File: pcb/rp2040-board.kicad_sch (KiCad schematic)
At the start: 4 parts, among them U1 RP2040, U2 W25Q128JVS

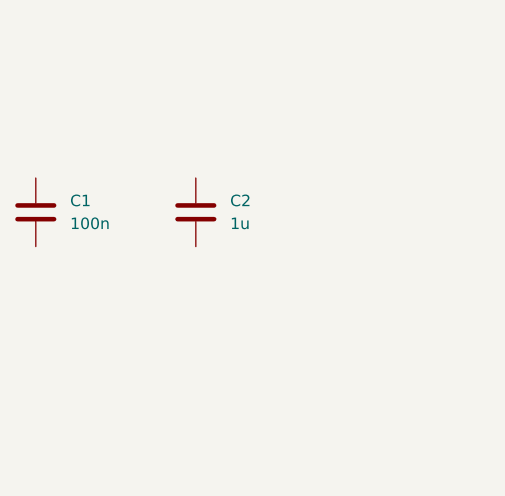
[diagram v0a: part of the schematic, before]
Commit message: add more parts to the BOM
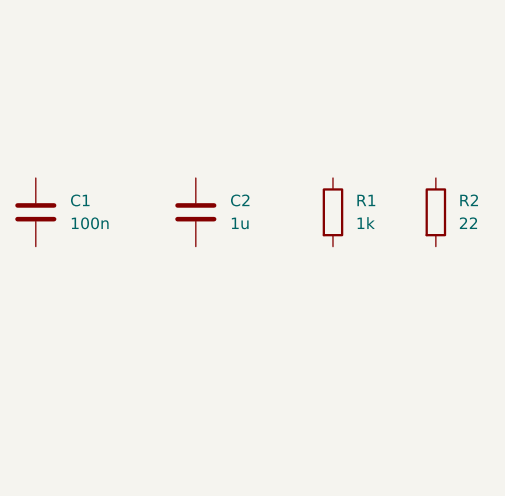
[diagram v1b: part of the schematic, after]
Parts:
- added R1: 1k, Resistor_SMD:R_0402_1005Metric, symbol Device:R
- added R2: 22, Resistor_SMD:R_0402_1005Metric, symbol Device:R
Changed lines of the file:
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@@
+    )
+  )
+  (symbol (lib_id "Device:R") (at 261.62 67.31 0) (unit 1)
+    (in_bom yes) (on_board yes) (dnp no) (fields_autoplaced)
+    (property "Reference" "R2" (at 264.16 66.04 0)
+      (effects (font (size 1.27 1.27)) (justify left))
+    )
+    (property "Value" "22" (at 264.16 68.58 0)
+      (effects (font (size 1.27 1.27)) (justify left))
+    )
+    (property "Footprint" "Resistor_SMD:R_0402_1005Metric" (at 259.842 67.31 90)
+      (effects (font (size 1.27 1.27)) hide)
+    )
+    (property "Datasheet" "https://datasheet.lcsc.com/lcsc/2205311900_UNI-ROYAL-Uniroyal-Elec-0402WGF220JTCE_C25092.pdf" (at 261.62 67.31 0)
+      (effects (font (size 1.27 1.27)) hide)
+    )
+    (property "LCSC Part" "C25092" (at 261.62 67.31 0)
+      (effects (font (size 1.27 1.27)) hide)
+    )
+    (pin "1")
+    (pin "2")
+    (instances
+      (project "rp2040-board"
+        (path "/75fe2d07-4ff9-4014-b967-9ecbb30e480e"
+          (reference "R2") (unit 1)
+        )
+      )
+    )
+  )
+  (symbol (lib_id "Device:R") (at 250.19 67.31 0) (unit 1)
+    (in_bom yes) (on_board yes) (dnp no) (fields_autoplaced)
+    (property "Reference" "R1" (at 252.73 66.04 0)
+      (effects (font (size 1.27 1.27)) (justify left))
+    )
+    (property "Value" "1k" (at 252.73 68.58 0)
+      (effects (font (size 1.27 1.27)) (justify left))
+    )
+    (property "Footprint" "Resistor_SMD:R_0402_1005Metric" (at 248.412 67.31 90)
+      (effects (font (size 1.27 1.27)) hide)
+    )
+    (property "Datasheet" "https://datasheet.lcsc.com/lcsc/2206010216_UNI-ROYAL-Uniroyal-Elec-0402WGF1001TCE_C11702.pdf" (at 250.19 67.31 0)
+      (effects (font (size 1.27 1.27)) hide)
+    )
+    (property "LCSC Part" "C11702" (at 250.19 67.31 0)
+      (effects (font (size 1.27 1.27)) hide)
+    )
+    (pin "1")
+    (pin "2")
+    (instances
+      (project "rp2040-board"
+        (path "/75fe2d07-4ff9-4014-b967-9ecbb30e480e"
+          (reference "R1") (unit 1)
+        )
+      )
     )
   )

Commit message: schematic wip
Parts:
- added C10, C11, C12, C3, C5, C6, C7, C8, C9: 100n, Capacitor_SMD:C_0402_1005Metric, symbol Device:C
- added C13, C4: 1u, Capacitor_SMD:C_0402_1005Metric, symbol Device:C
- added R3: 22, Resistor_SMD:R_0402_1005Metric, symbol Device:R
- added R4: DNP, Resistor_SMD:R_0402_1005Metric, symbol Device:R
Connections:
- net QSPI_SS: now reaches U2.1 (~{CS})
- net QSPI_SS: now also R1.1, U1.56 (QSPI_SS), R4.2
- net QSPI_SD1: now reaches U2.2 (DO(IO1))
- net QSPI_SD1: now also U1.55 (QSPI_SD1)
- net QSPI_SD2: now reaches U2.3 (IO2)
- net QSPI_SD2: now also U1.54 (QSPI_SD2)
- net GND: now reaches U2.4 (GND)
- net GND: now also C1.2, C2.2, U1.57 (GND), C10.2, C11.2, C12.2, C13.2, C3.2, C4.2, C5.2, C6.2, C7.2, C8.2, C9.2
- net QSPI_SD0: now reaches U2.5 (DI(IO0))
- net QSPI_SD0: now also U1.53 (QSPI_SD0)
- net QSPI_SCLK: now reaches U2.6 (CLK)
- net QSPI_SCLK: now also U1.52 (QSPI_SCLK)
- net QSPI_SD3: now reaches U2.7 (IO3)
- net QSPI_SD3: now also U1.51 (QSPI_SD3)
- net +3V3: now reaches U2.8 (VCC)
- net +3V3: now also C1.1, C2.1, U1.1 (IOVDD), U1.10 (IOVDD), U1.22 (IOVDD), U1.33 (IOVDD), U1.42 (IOVDD), U1.43 (ADC_AVDD), U1.44 (VREG_IN), U1.48 (USB_VDD), U1.49 (IOVDD), C10.1, C11.1, C12.1, C13.1, C6.1, C7.1, C8.1, C9.1, R4.1
- net USB_DP: now reaches R2.1
- net at R2.2: now also U1.47 (USB_DP)
- net #USB_BOOT: now reaches R1.2
- net +1V1: now reaches U1.23 (DVDD), U1.50 (DVDD)
- net +1V1: now also U1.45 (VREG_VOUT), C3.1, C4.1, C5.1
- net at U1.46 (USB_DM): now also R3.2
- new net USB_DM: R3.1
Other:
- moved on the sheet: C1, C2, R1, R2, U1, U2

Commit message: schematic wip
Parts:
- added C14, C15: 18p, Capacitor_SMD:C_0402_1005Metric, symbol Device:C
- added R5: 1k, Resistor_SMD:R_0402_1005Metric, symbol Device:R
- added SW1: USB Boot, Button_Switch_SMD:SW_Push_1P1T_XKB_TS-1187A, symbol Switch:SW_SPST
- added Y1: 12MHz, Crystal:Crystal_SMD_3225-4Pin_3.2x2.5mm, symbol Device:Crystal_GND24
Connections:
- net #USB_BOOT: now also SW1.2 (B)
- net GND: now also C14.2, C15.2, SW1.1 (A), Y1.2, Y1.4
- net at U1.20 (XIN): now also C14.1, Y1.1
- net at U1.21 (XOUT): now also R5.1
- new net: C15.1, R5.2, Y1.3

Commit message: schematic wip
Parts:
- added C16: 100n, Capacitor_SMD:C_0402_1005Metric, symbol Device:C
- added C17: 1u, Capacitor_SMD:C_0402_1005Metric, symbol Device:C
- added D1: Yellow, LED_SMD:LED_0603_1608Metric, symbol Device:LED
- added D2: Red, LED_SMD:LED_0603_1608Metric, symbol Device:LED
- added R6, R7: 330, Resistor_SMD:R_0402_1005Metric, symbol Device:R
- added SW2: Reset, Button_Switch_SMD:SW_Push_1P1T_XKB_TS-1187A, symbol Switch:SW_SPST
- added U3: SP485EEN-L/TR, Package_SO:SOIC-8_3.9x4.9mm_P1.27mm, symbol Interface_UART:MAX485E
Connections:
- net GND: now also U1.19 (TESTEN), C16.2, C17.2, D1.1 (K), D2.1 (K), SW2.1 (A), U3.5 (GND)
- net RUN: now reaches U1.26 (RUN)
- net RUN: now also SW2.2 (B)
- net LED_D2: now reaches U1.36 (GPIO24)
- net LED_D2: now also R7.2
- net LED_D1: now reaches U1.37 (GPIO25)
- net LED_D1: now also R6.2
- new net: D1.2 (A), R6.1
- new net: D2.2 (A), R7.1
- new net +5V: C16.1, C17.1, U3.8 (VCC)
- new net RS485_RE_NDE: U3.2 (~{RE}), U3.3 (DE)
- new net RS485_RXD: U3.1 (RO)
- new net RS485_TXD: U3.4 (DI)

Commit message: schematic wip
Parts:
- added C18, C19: 10u, Capacitor_SMD:C_0603_1608Metric, symbol Device:C
- added D3: SS14, Diode_SMD:D_SMA, symbol Device:D_Schottky
- added J1: Conn_ARM_JTAG_SWD_10, symbol Connector:Conn_ARM_JTAG_SWD_10
- added J2: USB_C_Receptacle_USB2.0_16P, Connector_USB:USB_C_Receptacle_G-Switch_GT-USB-7010ASV, symbol Connector:USB_C_Receptacle_USB2.0_16P
- added R8: 1k, Resistor_SMD:R_0402_1005Metric, symbol Device:R
- added U4: XC6206P332MR, Package_TO_SOT_SMD:SOT-23-3, symbol Regulator_Linear:XC6206PxxxMR
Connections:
- net +3V3: now also C18.1, J1.1 (VTref), U4.2 (VO)
- net +5V: now also C19.1, D3.1 (K), U4.3 (VI)
- net GND: now also C18.2, C19.2, J1.3 (GND), J1.5 (GND), J1.9 (GNDDetect), J2.A1 (GND), J2.A12 (GND), J2.B1 (GND), J2.B12 (GND), J2.S1 (SHIELD), U4.1 (GND)
- net RUN: now also J1.10 (~{RESET}), R8.1; no longer SW2.2 (B)
- net USB_DM: now also J2.A7 (D-), J2.B7 (D-)
- net USB_DP: now also J2.A6 (D+), J2.B6 (D+)
- net SWCLK: now reaches U1.24 (SWCLK)
- net SWCLK: now also J1.4 (SWCLK/TCK)
- net SWD: now reaches U1.25 (SWD)
- net SWD: now also J1.2 (SWDIO/TMS)
- net SWO: now reaches U1.27 (GPIO16)
- net SWO: now also J1.6 (SWO/TDO)
- new net: R8.2, SW2.2 (B)
- new net VBUS: D3.2 (A), J2.A4 (VBUS), J2.A9 (VBUS), J2.B4 (VBUS), J2.B9 (VBUS)
- no-connect marks 0 -> 5

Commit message: schematic wip
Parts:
- added D4, D5: SS34, Diode_SMD:D_SMA, symbol Device:D_Schottky
- added J3: RS485, Connector_PinHeader_2.54mm:PinHeader_1x03_P2.54mm_Vertical, symbol Connector_Generic:Conn_01x03
- added R10, R11: 1R, Resistor_SMD:R_0603_1608Metric, symbol Device:R
- added R9: 0, Resistor_SMD:R_0402_1005Metric, symbol Device:R
- added SW6: RotaryEncoder_Switch, symbol Device:RotaryEncoder_Switch
- D3: value SS14 -> SS34; LCSC Part C2480 -> C8678
- J1: footprint (none) -> Connector_PinHeader_1.27mm:PinHeader_2x05_P1.27mm_Vertical_SMD
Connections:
- net +5V: now also R9.1
- net GND: now also D3.2 (A), D4.2 (A), D5.2 (A), SW6.C, SW6.S2
- net VBUS: now also R9.2; no longer D3.2 (A)
- net at U3.6 (A): now also D4.1 (K), R11.2
- net at U3.7 (B): now also D5.1 (K), R10.2
- net RE_A: now reaches U1.32 (GPIO21)
- net RE_A: now also SW6.A
- net RE_B: now reaches U1.34 (GPIO22)
- net RE_B: now also SW6.B
- net RE_SW: now reaches U1.35 (GPIO23)
- net RE_SW: now also SW6.S1
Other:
- moved on the sheet: C1, C10, C11, C12, C13, C14, C15, C16, C17, C18, C19, C2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

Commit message: schematic wip
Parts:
- added J4: ELRS, Connector_PinHeader_2.54mm:PinHeader_1x04_P2.54mm_Vertical, symbol Connector_Generic:Conn_01x04
- added J5: OLED, Connector_PinHeader_2.54mm:PinHeader_1x04_P2.54mm_Vertical, symbol Connector_Generic:Conn_01x04
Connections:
- net +3V3: now also J5.2 (Pin_2)
- net +5V: now also J4.3 (Pin_3)
- net GND: now also J4.4 (Pin_4), J5.1 (Pin_1)
- net OLED_SCK: now reaches U1.28 (GPIO17)
- net OLED_SCK: now also J5.3 (Pin_3)
- net OLED_SDA: now reaches U1.29 (GPIO18)
- net OLED_SDA: now also J5.4 (Pin_4)
- net ELRS_TX: now reaches U1.30 (GPIO19)
- net ELRS_TX: now also J4.1 (Pin_1)
- net ELRS_RX: now reaches U1.31 (GPIO20)
- net ELRS_RX: now also J4.2 (Pin_2)

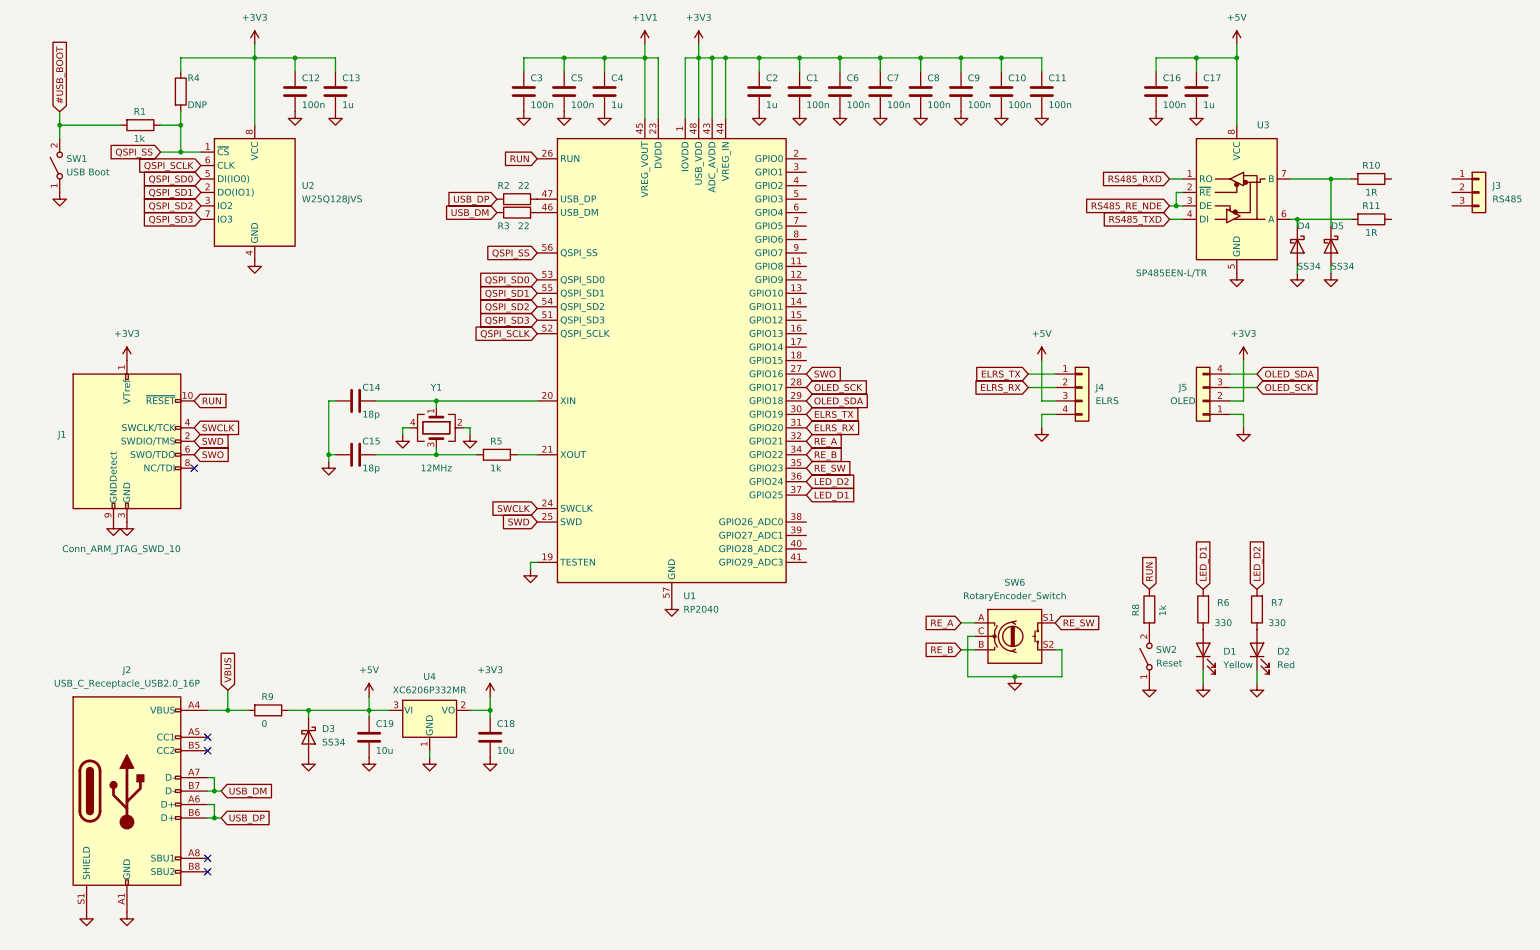
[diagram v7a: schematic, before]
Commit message: schematic finalization, pcb draft
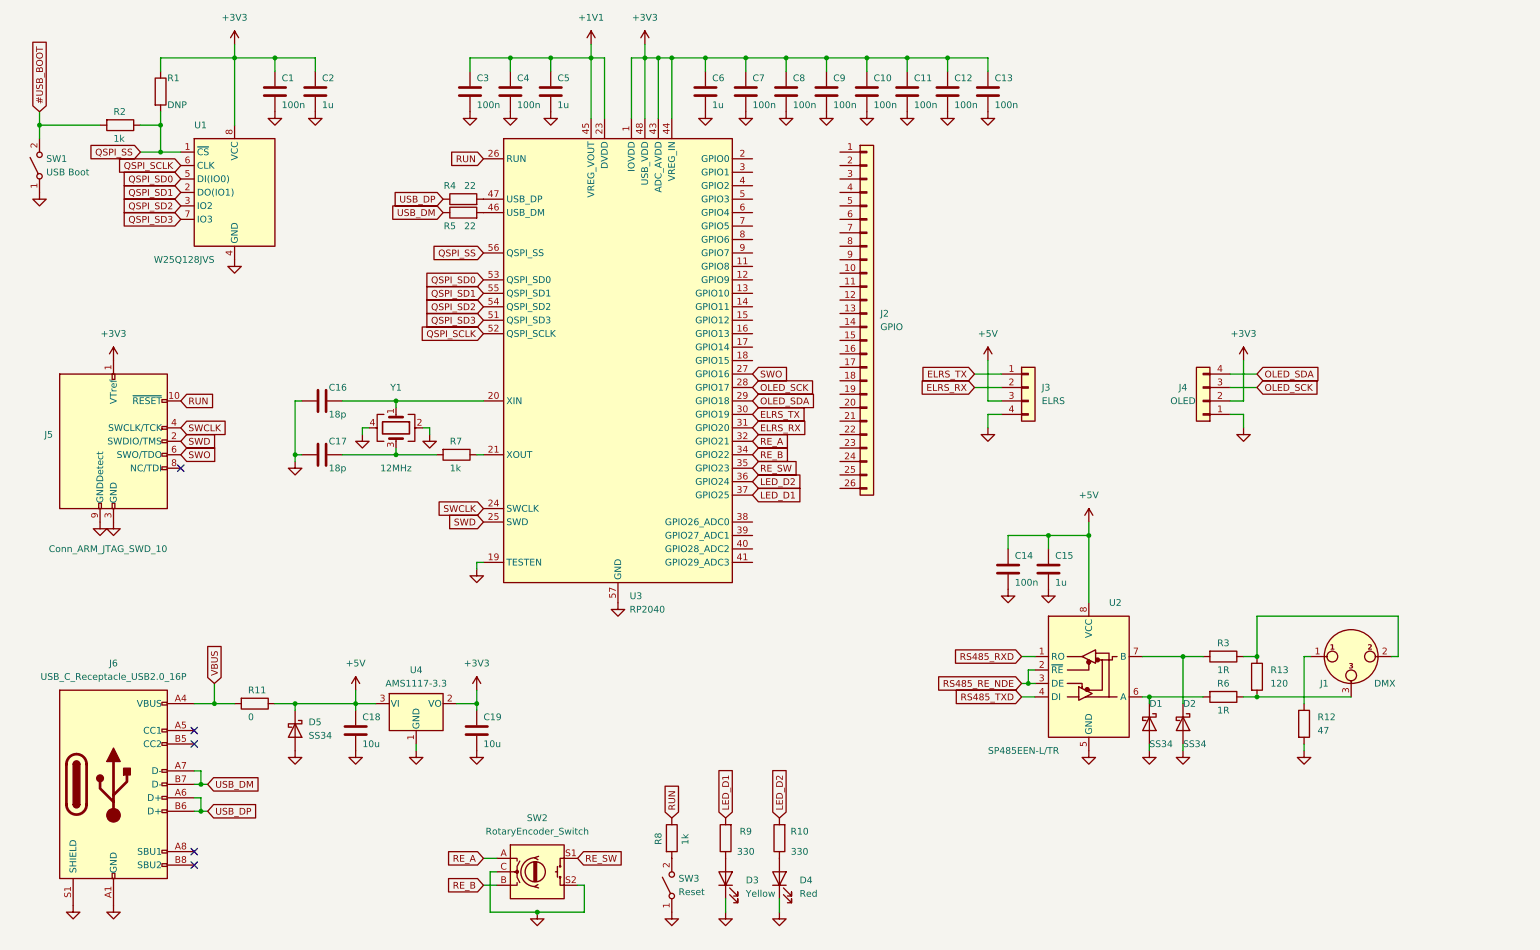
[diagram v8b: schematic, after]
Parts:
- removed J3: RS485, Connector_PinHeader_2.54mm:PinHeader_1x03_P2.54mm_Vertical, symbol Connector_Generic:Conn_01x03
- added J1: DMX, Connector_Audio:Jack_XLR_Neutrik_NC3FAAH_Horizontal, symbol Connector_Audio:XLR3
- added J2: GPIO, Connector_PinHeader_2.54mm:PinHeader_1x26_P2.54mm_Vertical, symbol Connector_Generic:Conn_01x26
- added R12: 47, Resistor_SMD:R_0603_1608Metric, symbol Device:R
- added R13: 120, Resistor_SMD:R_1206_3216Metric, symbol Device:R
- SW2: renamed from SW6; footprint (none) -> Rotary_Encoder:RotaryEncoder_Bourns_Vertical_PEC12R-3x17F-Sxxxx
- U4: value XC6206P332MR -> AMS1117-3.3; footprint Package_TO_SOT_SMD:SOT-23-3 -> Package_TO_SOT_SMD:SOT-223; LCSC Part C5446 -> C6186
- renumbered C12 to C1, C8 to C10, C9 to C11, C10 to C12, C11 to C13, C16 to C14, C17 to C15, C14 to C16, C15 to C17, C19 to C18, C18 to C19, C13 to C2, C5 to C4, C4 to C5, C2 to C6, C1 to C7, C6 to C8, C7 to C9, D4 to D1, D5 to D2, D1 to D3, D2 to D4, D3 to D5, J4 to J3, J5 to J4, J1 to J5, J2 to J6, R4 to R1, R7 to R10, R9 to R11, R1 to R2, R10 to R3, R2 to R4, R3 to R5, R11 to R6, R5 to R7, R6 to R9, SW2 to SW3, U2 to U1, U3 to U2, U1 to U3
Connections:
- net GND: now also R12.2
- net at R6.1: now also J1.3, R13.2
- net at R3.1: now also J1.2, R13.1
- new net: J1.1, R12.1
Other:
- moved on the sheet: C1, C10, C11, C12, C13, C14, C15, C16, C17, C18, C19, C2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
